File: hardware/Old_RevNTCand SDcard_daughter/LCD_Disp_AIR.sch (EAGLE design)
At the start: 11 parts

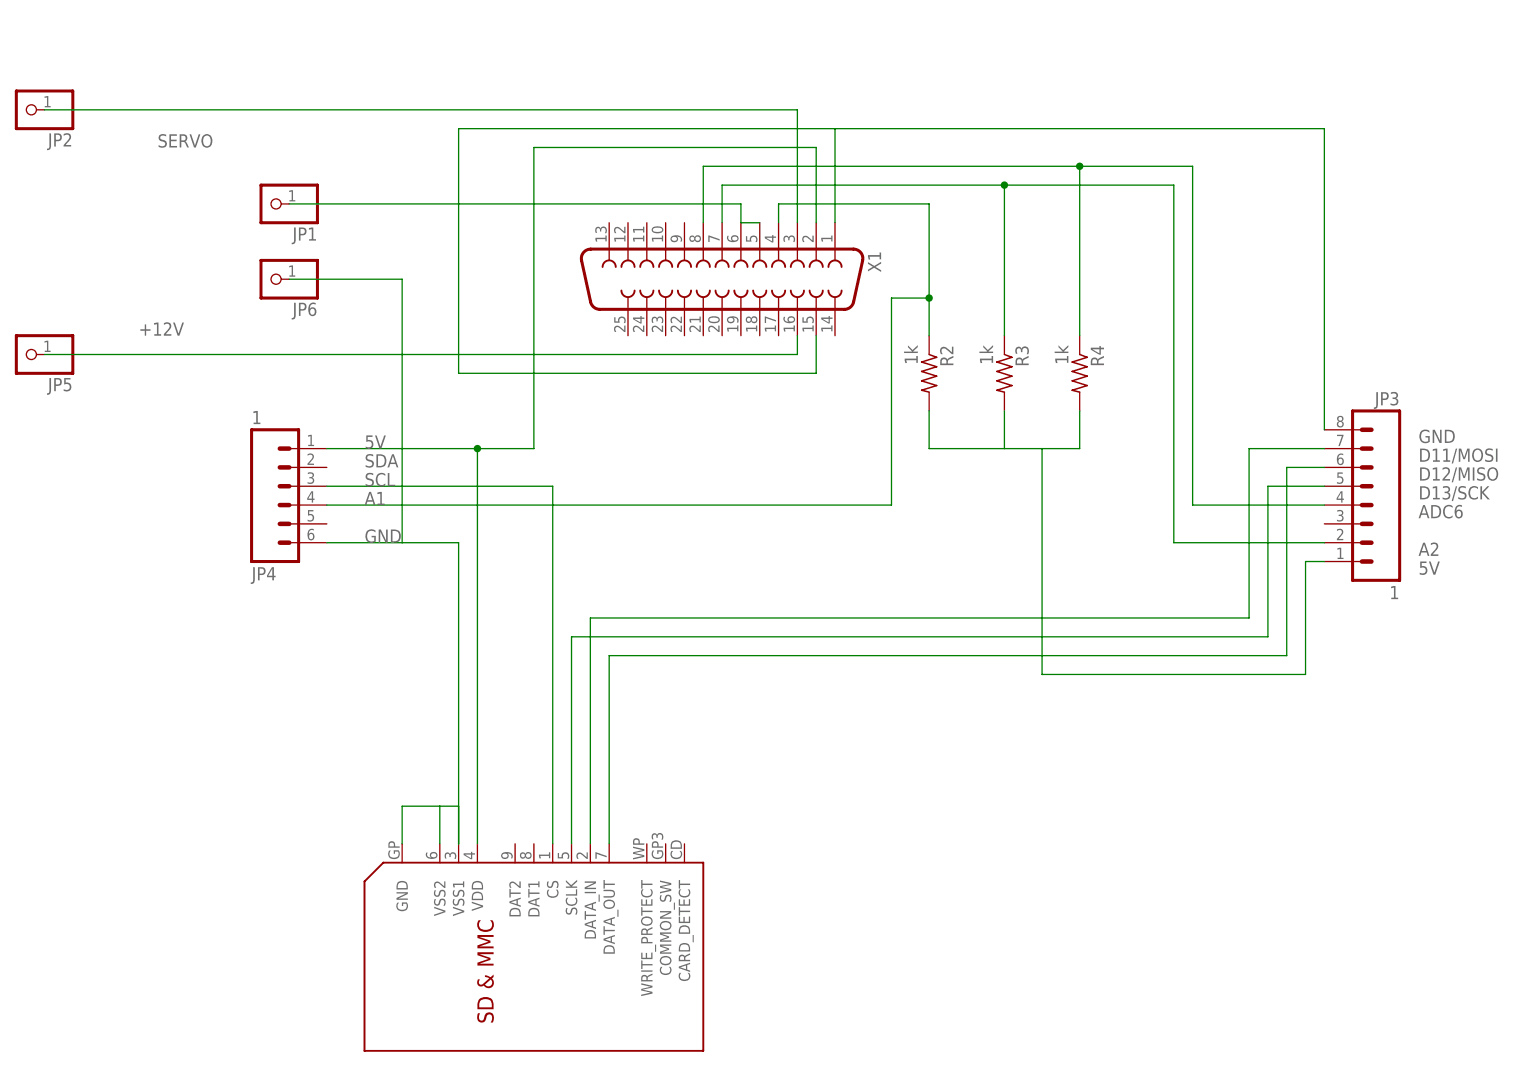
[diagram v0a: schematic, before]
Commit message: added schematic for use as solder controller
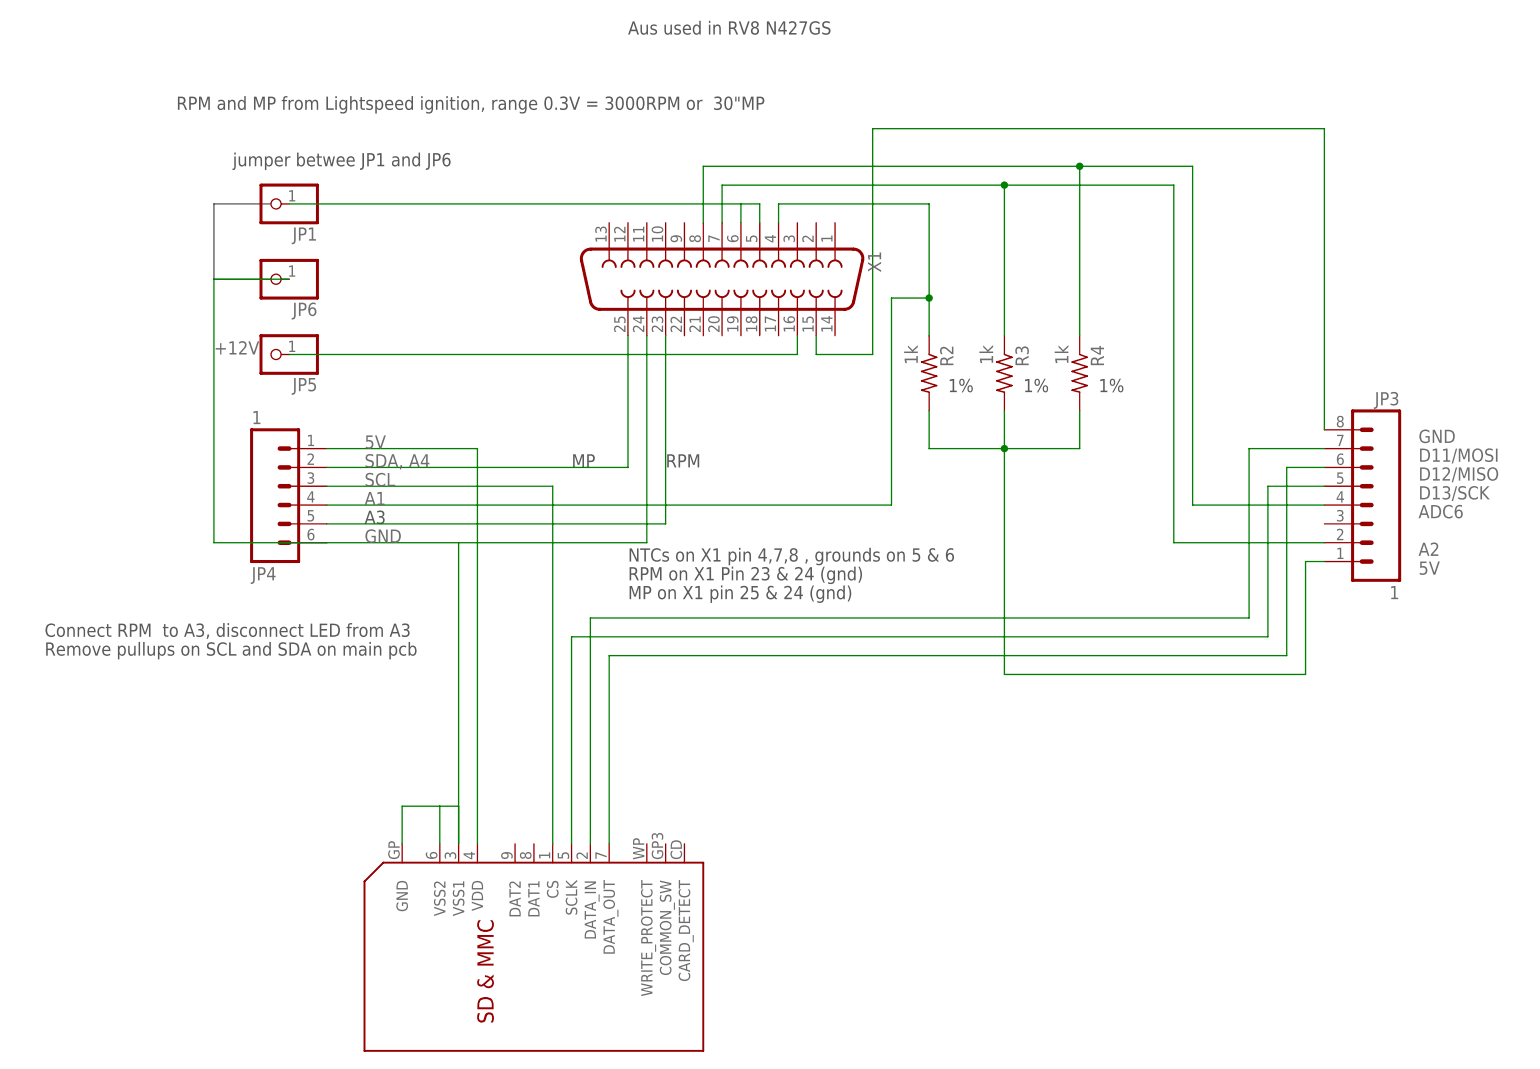
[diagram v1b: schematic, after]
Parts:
- removed JP2: (no value), adafruit:PINHD-1X1
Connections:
- removed net SERVO: JP2.1, X1.3
- new net N$5: JP4.5, X1.23
- new net N$6: JP4.2, X1.25
- net GND: now also X1.24
- net N$4: no longer X1.1
- net VDD: no longer X1.2
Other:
- note added: "1%"
- note added: "A3"
- note added: "Aus used in RV8 N427GS"
- note added: "Connect RPM to A3, disconnect LED from A3"
- note added: "MP"
- note added: "MP on X1 pin 25 & 24 (gnd)"
- note added: "NTCs on X1 pin 4,7,8 , grounds on 5 & 6"
- note added: "RPM"
- note added: "RPM and MP from Lightspeed ignition, range 0.3V = 3000RPM or 30"MP"
- note added: "RPM on X1 Pin 23 & 24 (gnd)"
- note added: "Remove pullups on SCL and SDA on main pcb"
- note added: "SDA, A4"
- note added: "jumper betwee JP1 and JP6"
- note removed: "SDA"
- moved on the sheet: JP5
